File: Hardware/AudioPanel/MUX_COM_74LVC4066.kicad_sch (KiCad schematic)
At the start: 51 parts, among them SW10 ~{RESET}, SW11 ~{RESET}, SW12 ~{RESET}, SW13 ~{RESET}, SW14 ~{RESET}, SW15 ~{RESET}, SW9 ~{RESET}, U45 MCP23017_ML, U61 74LVC4066BQ, U62 74LVC4066BQ, U63 74LVC4066BQ, U64 74LVC4066BQ, U65 74LVC4066BQ, U66 74LVC4066BQ, U67 74LVC4066BQ, U68 74LVC4066BQ, U69 74LVC4066BQ, U70 74LVC4066BQ, U71 74LVC4066BQ, U72 74LVC4066BQ, U73 74LVC4066BQ, U74 74LVC4066BQ, U75 74LVC4066BQ, U76 74LVC4066BQ, U77 74LVC4066BQ, U78 74LVC4066BQ, U79 74LVC4066BQ, U80 74LVC4066BQ, U81 74LVC4066BQ, U82 74LVC4066BQ, U83 74LVC4066BQ, U84 74LVC4066BQ, U85 74LVC4066BQ, U86 74LVC4066BQ, U87 74LVC4066BQ, U88 74LVC4066BQ, U89 74LVC4066BQ, U90 74LVC4066BQ, U91 MCP23017_ML, U92 MCP23017_ML, U93 MCP23017_ML, U94 MCP23017_ML, U95 MCP23017_ML, U96 MCP23017_ML

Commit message: Added DSP chips, practicing with bus lines
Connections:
- net CTS_1 renamed CTS.1
- net CTS_2 renamed CTS.2
- net CTS_3 renamed CTS.3
- net CTS_4 renamed CTS.4
- net CTS_5 renamed CTS.5
- net RTS_1 renamed RTS.1
- net RTS_2 renamed RTS.2
- net RTS_3 renamed RTS.3
- net RTS_4 renamed RTS.4
- net RTS_5 renamed RTS.5
- net RXD_1 renamed RXD1
- net RXD_2 renamed RXD2
- net RXD_3 renamed RXD3
- net RXD_4 renamed RXD4
- net RXD_5 renamed RXD5
- net TXD_1 renamed TXD1
- net TXD_2 renamed TXD2
- net TXD_3 renamed TXD3
- net TXD_4 renamed TXD4
- net TXD_5 renamed TXD5

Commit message: Added group labels
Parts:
- removed U61, U62, U63, U64, U65, U66, U67, U68, U69, U70, U71, U72, U73, U74, U75, U76, U77, U78, U79, U80, U81, U82, U83, U84, U85, U86, U87, U88, U89, U90: 74LVC4066BQ, Package_SO:SO-14_3.9x8.65mm_P1.27mm, symbol Analog_Switch:CD4066BM
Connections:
- net CTS.1 renamed 480_COM.CTS
- net CTS.2 renamed 710_COM.CTS
- net CTS.3 renamed 700_COM.CTS
- net CTS.4 renamed EXTRA_COM.CTS
- net CTS.5 renamed PC_COM.CTS
- net RTS.1 renamed 480_COM.RTS
- net RTS.2 renamed 710_COM.RTS
- net RTS.3 renamed 700_COM.RTS
- net RTS.4 renamed EXTRA_COM.RTS
- net RTS.5 renamed PC_COM.RTS
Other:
- added sheet Switch Matrix (MATRIX_5X5.kicad_sch)
- moved on the sheet: C335, C336, C337, C338, C339, C340, C341, SW10, SW11, SW12, SW13, SW14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

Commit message: Simplified COM switching, added USB-232
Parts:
- removed C336, C337, C338, C339, C340: 100nF, symbol Device:C_Small
- removed SW10, SW11, SW12, SW13, SW14: ~{RESET}, Button_Switch_SMD:SW_SPST_TL3342, symbol Switch:SW_Push
- removed U91, U92, U93, U94, U95: MCP23017_ML, Package_DFN_QFN:QFN-28-1EP_6x6mm_P0.65mm_EP4.25x4.25mm, symbol Interface_Expansion:MCP23017_ML
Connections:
- net A10 is gone; now on net 480_COM.TX: U45.17 (GPA0)
- net A2 is gone; now on net 480_COM.RX: U45.25 (GPB0)
- net A3 is gone; now on net 710_COM.RX: U45.26 (GPB1)
- net A4 is gone; now on net 700_COM.RX: U45.27 (GPB2)
- net A5 is gone; now on net EXTRA_COM.RX: U45.28 (GPB3)
- net B1 is gone; now on net 710_COM.TX: U45.18 (GPA1)
- net B3 is gone; now on net 700_COM.TX: U45.19 (GPA2)
- net B4 is gone; now on net EXTRA_COM.TX: U45.20 (GPA3)
- net 480_COM.CTS: now also U96.17 (GPA0); no longer U96.25 (GPB0)
- net 480_COM.RTS: now also U96.25 (GPB0); no longer U96.17 (GPA0)
- net 700_COM.CTS: now also U96.19 (GPA2); no longer U96.27 (GPB2)
- net 700_COM.RTS: now also U96.27 (GPB2); no longer U96.19 (GPA2)
- net 710_COM.CTS: now also U96.18 (GPA1); no longer U96.26 (GPB1)
- net 710_COM.RTS: now also U96.26 (GPB1); no longer U96.18 (GPA1)
- net EXTRA_COM.CTS: now also U96.20 (GPA3); no longer U96.28 (GPB3)
- net EXTRA_COM.RTS: now also U96.28 (GPB3); no longer U96.20 (GPA3)
- net PC2_COM.RTS: now reaches U96.2 (GPB5)
- net PC2_COM.CTS: now reaches U96.22 (GPA5)
- net PC3_COM.CTS: now reaches U96.23 (GPA6)
- net PC4_COM.CTS: now reaches U96.24 (GPA7)
- net PC3_COM.RTS: now reaches U96.3 (GPB6)
- net PC4_COM.RTS: now reaches U96.4 (GPB7)
- net A6 renamed PC1_COM.RX
- net A7 renamed PC2_COM.RX
- net A8 renamed PC3_COM.RX
- net A9 renamed PC4_COM.RX
- net B5 renamed PC1_COM.TX
- net B6 renamed PC2_COM.TX
- net B7 renamed PC3_COM.TX
- net B8 renamed PC4_COM.TX
- net PC_COM.CTS renamed PC1_COM.RTS
- net PC_COM.RTS renamed PC1_COM.CTS
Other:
- removed sheet Switch Matrix
- moved on the sheet: C335, C341, SW15, SW9, U45, U96

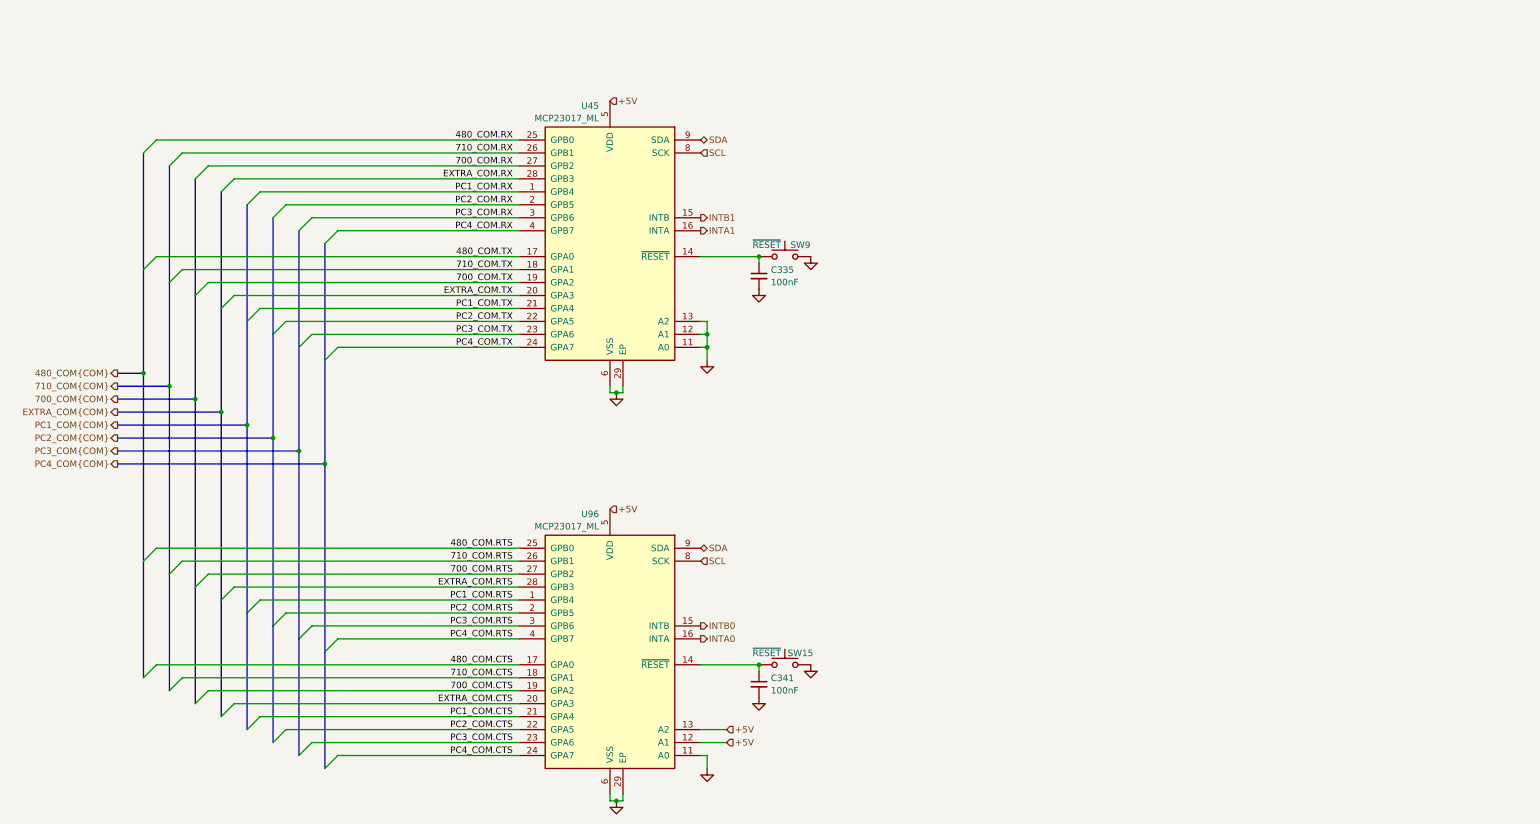
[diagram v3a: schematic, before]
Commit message: Added ideal diode controller to main power input
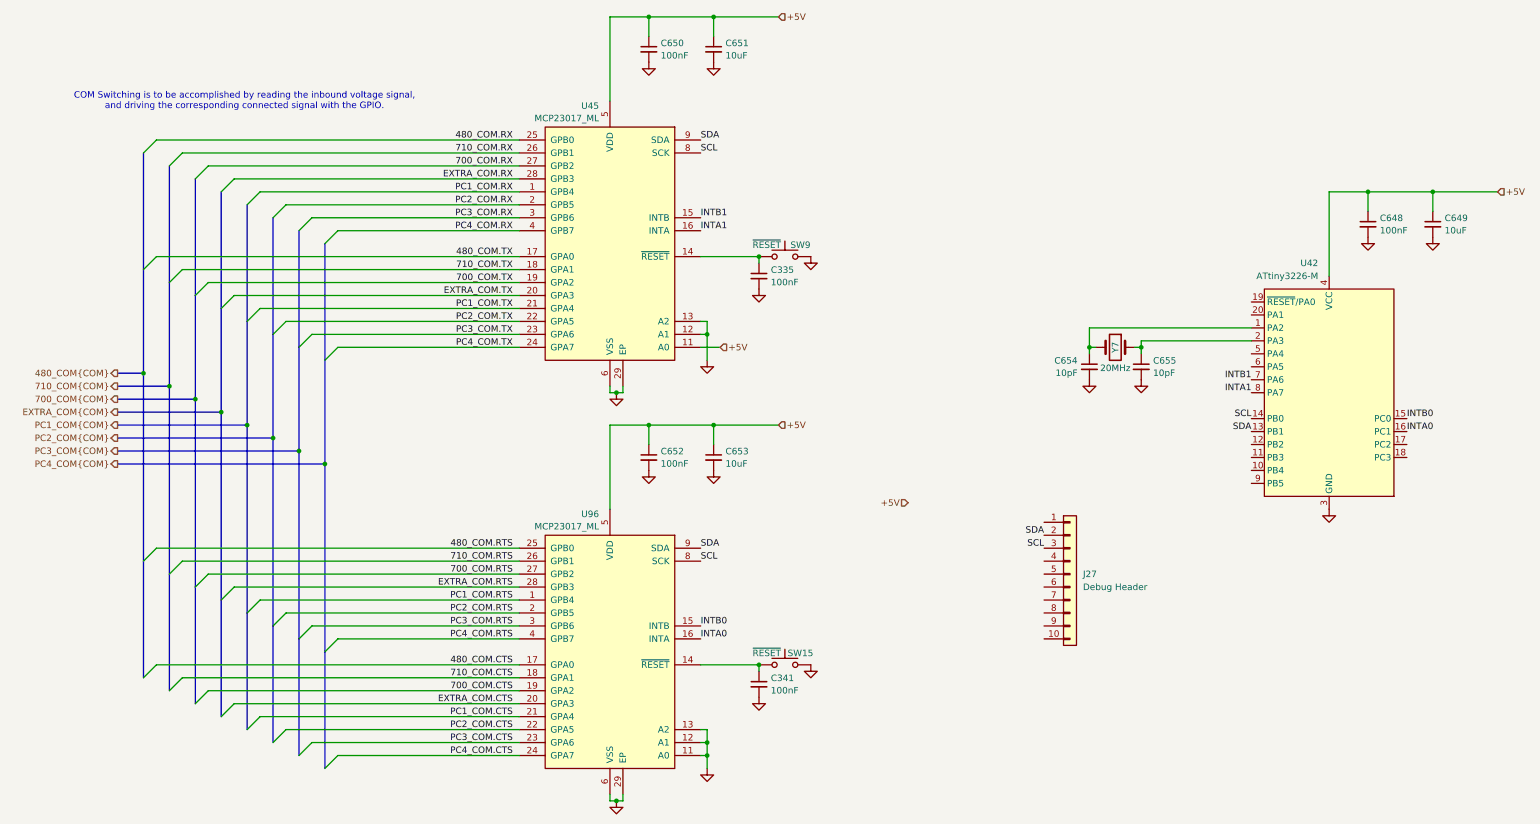
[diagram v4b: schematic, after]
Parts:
- added C648, C650, C652: 100nF, symbol Device:C_Small
- added C649, C651, C653: 10uF, symbol Device:C_Small
- added C654, C655: 10pF, symbol Device:C_Small
- added J27: Debug Header, symbol Connector_Generic:Conn_01x10
- added U42: ATtiny3226-M, Package_DFN_QFN:VQFN-20-1EP_3x3mm_P0.4mm_EP1.7x1.7mm, symbol MCU_Microchip_ATtiny:ATtiny3226-M
- added Y7: 20MHz, symbol Device:Crystal
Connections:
- net +5V: now also U45.11 (A0), C648.1, C649.1, C650.1, C651.1, C652.1, C653.1, U42.4 (VCC); no longer U96.12 (A1), U96.13 (A2)
- net GND: now also U96.12 (A1), U96.13 (A2), C648.2, C649.2, C650.2, C651.2, C652.2, C653.2, C654.2, C655.2, U42.21 (GND), U42.3 (GND); no longer U45.11 (A0)
- net INTA0: now also U42.16 (PC1)
- net INTA1: now also U42.8 (PA7)
- net INTB0: now also U42.15 (PC0)
- net INTB1: now also U42.7 (PA6)
- net SCL: now also J27.3 (Pin_3), U42.14 (PB0)
- net SDA: now also J27.2 (Pin_2), U42.13 (PB1)
- new net: C654.1, U42.1 (PA2), Y7.2
- new net: C655.1, U42.2 (PA3), Y7.1
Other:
- note added: "COM Switching is to be accomplished by reading the inbound voltage signal, and driving the corresponding connected signal with the GPIO."

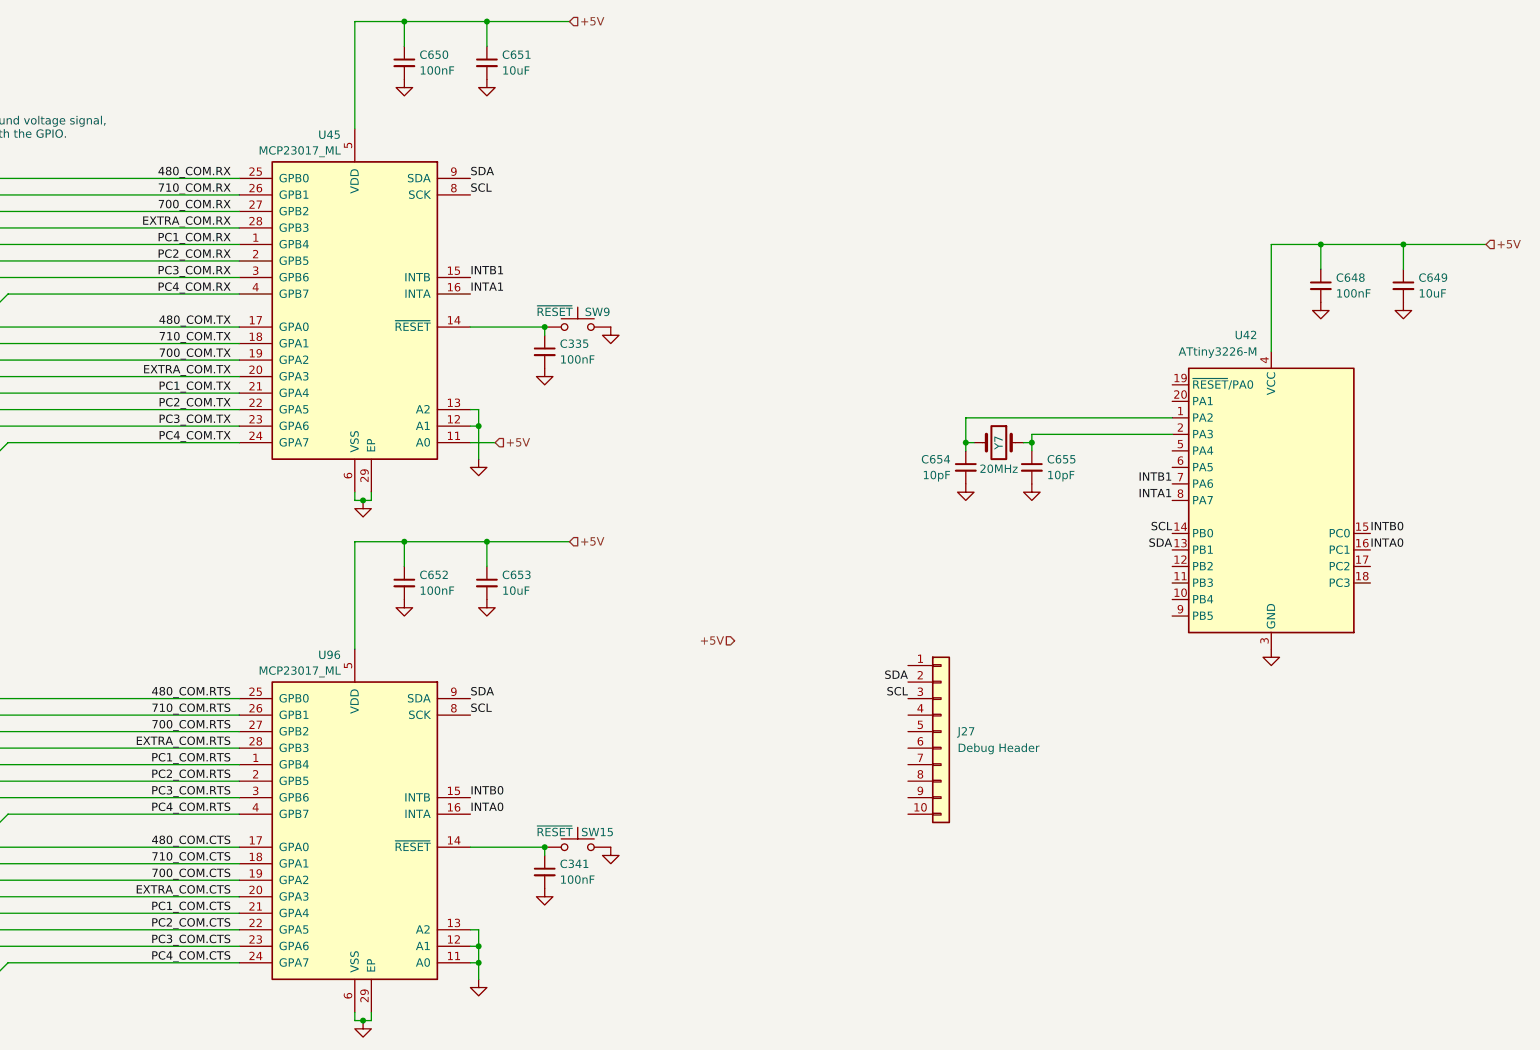
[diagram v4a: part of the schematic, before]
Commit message: Realized that I need to rethink how I'm going to mix the radio audio with the stereo audio
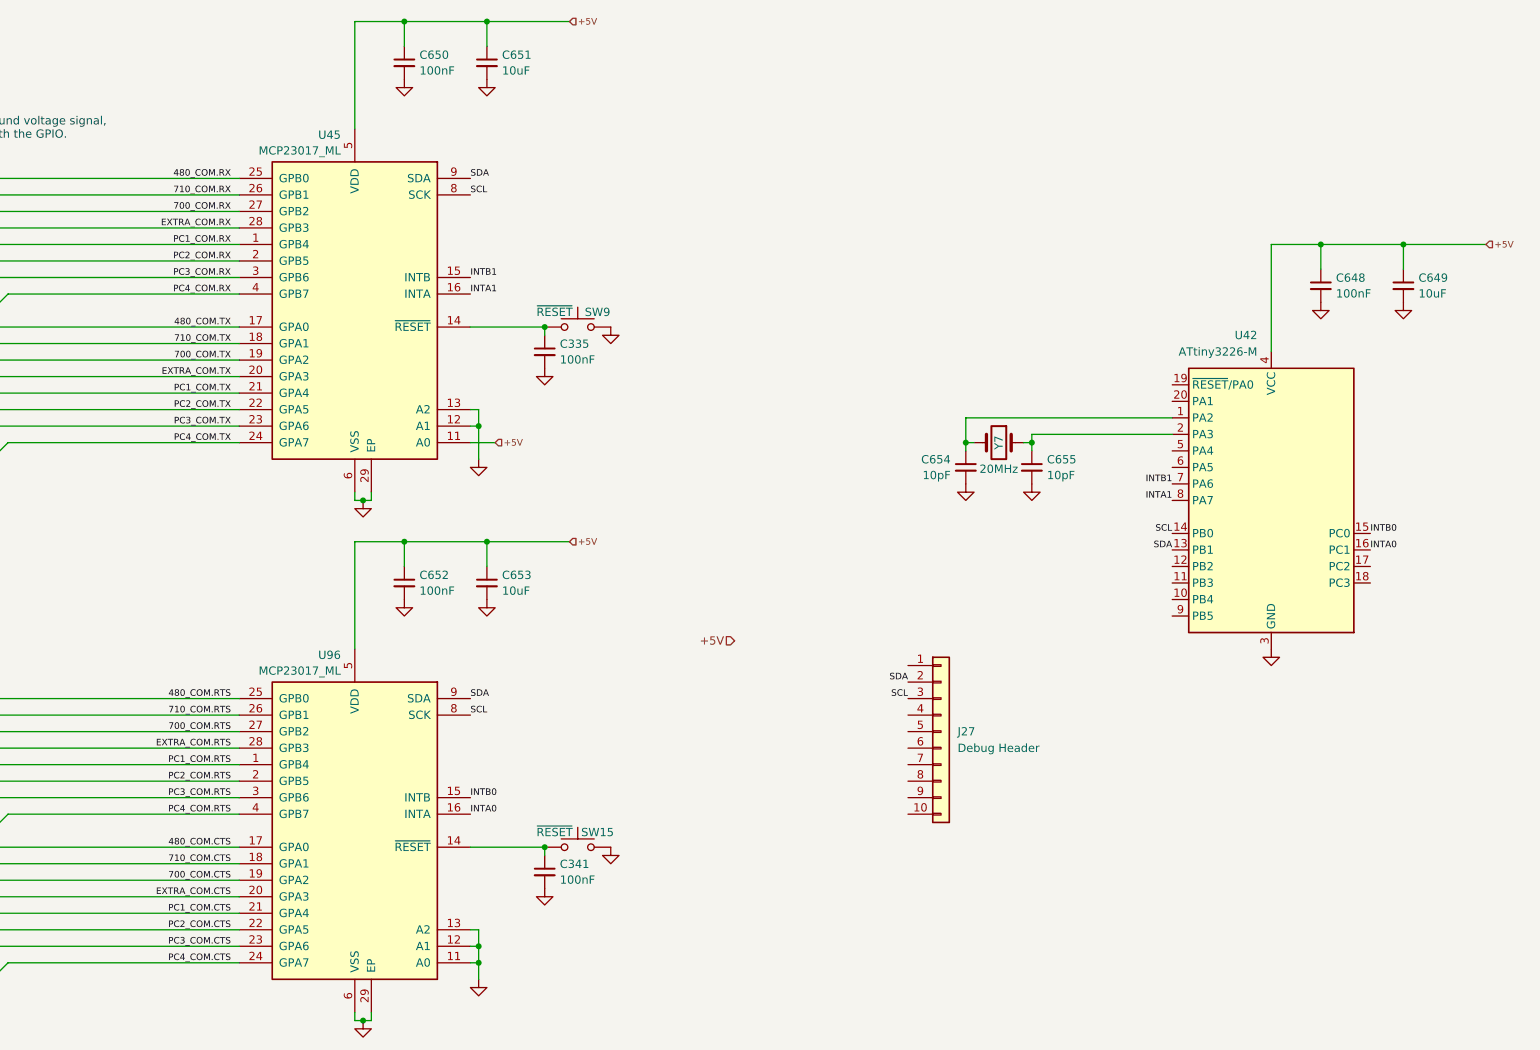
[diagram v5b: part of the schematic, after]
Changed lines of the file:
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@@
 		(effects
 			(font
-				(size 1.27 1.27)
+				(size 1 1)
 			)
 			(justify left bottom)
@@
 		(effects
 			(font
-				(size 1.27 1.27)
+				(size 1 1)
 			)
 			(justify right bottom)
@@
 		(effects
 			(font
-				(size 1.27 1.27)
+				(size 1 1)
 			)
 			(justify right bottom)
@@
 		(effects
 			(font
-				(size 1.27 1.27)
+				(size 1 1)
 			)
 			(justify right bottom)
@@
 		(effects
 			(font
-				(size 1.27 1.27)
+				(size 1 1)
 			)
 			(justify right bottom)
@@
 		(effects
 			(font
-				(size 1.27 1.27)
+				(size 1 1)
 			)
 			(justify right bottom)
@@
 		(effects
 			(font
-				(size 1.27 1.27)
+				(size 1 1)
 			)
 			(justify right bottom)
@@
 		(effects
 			(font
-				(size 1.27 1.27)
+				(size 1 1)
 			)
 			(justify right bottom)
@@
 		(effects
 			(font
-				(size 1.27 1.27)
+				(size 1 1)
 			)
 			(justify right bottom)
@@
 		(effects
 			(font
-				(size 1.27 1.27)
+				(size 1 1)
 			)
 			(justify right bottom)
@@
 		(effects
 			(font
-				(size 1.27 1.27)
+				(size 1 1)
 			)
 			(justify right bottom)
@@
 		(effects
 			(font
-				(size 1.27 1.27)
+				(size 1 1)
 			)
 			(justify right bottom)
@@
 		(effects
 			(font
-				(size 1.27 1.27)
+				(size 1 1)
 			)
 			(justify right bottom)
@@
 		(effects
 			(font
-				(size 1.27 1.27)
+				(size 1 1)
 			)
 			(justify right bottom)
@@
 		(effects
 			(font
-				(size 1.27 1.27)
+				(size 1 1)
 			)
 			(justify right bottom)
@@
 		(effects
 			(font
-				(size 1.27 1.27)
+				(size 1 1)
 			)
 			(justify right bottom)
@@
 		(effects
 			(font
-				(size 1.27 1.27)
+				(size 1 1)
 			)
 			(justify right bottom)
@@
 		(effects
 			(font
-				(size 1.27 1.27)
+				(size 1 1)
 			)
 			(justify left bottom)
@@
 		(effects
 			(font
-				(size 1.27 1.27)
+				(size 1 1)
 			)
 			(justify left bottom)
@@
 		(effects
 			(font
-				(size 1.27 1.27)
+				(size 1 1)
 			)
 			(justify right bottom)
@@
 		(effects
 			(font
-				(size 1.27 1.27)
+				(size 1 1)
 			)
 			(justify right bottom)
@@
 		(effects
 			(font
-				(size 1.27 1.27)
+				(size 1 1)
 			)
 			(justify right bottom)
@@
 		(effects
 			(font
-				(size 1.27 1.27)
+				(size 1 1)
 			)
 			(justify right bottom)
@@
 		(effects
 			(font
-				(size 1.27 1.27)
+				(size 1 1)
 			)
 			(justify right bottom)
@@
 		(effects
 			(font
-				(size 1.27 1.27)
+				(size 1 1)
 			)
 			(justify right bottom)
@@
 		(effects
 			(font
-				(size 1.27 1.27)
+				(size 1 1)
 			)
 			(justify right bottom)
@@
 		(effects
 			(font
-				(size 1.27 1.27)
+				(size 1 1)
 			)
 			(justify right bottom)
@@
 		(effects
 			(font
-				(size 1.27 1.27)
+				(size 1 1)
 			)
 			(justify right bottom)
@@
 		(effects
 			(font
-				(size 1.27 1.27)
+				(size 1 1)
 			)
 			(justify left bottom)
@@
 		(effects
 			(font
-				(size 1.27 1.27)
+				(size 1 1)
 			)
 			(justify right bottom)
@@
 		(effects
 			(font
-				(size 1.27 1.27)
+				(size 1 1)
 			)
 			(justify right bottom)
@@
 		(effects
 			(font
-				(size 1.27 1.27)
+				(size 1 1)
 			)
 			(justify left bottom)
@@
 		(effects
 			(font
-				(size 1.27 1.27)
+				(size 1 1)
 			)
 			(justify left bottom)
@@
 		(effects
 			(font
-				(size 1.27 1.27)
+				(size 1 1)
 			)
 			(justify right bottom)
@@
 		(effects
 			(font
-				(size 1.27 1.27)
+				(size 1 1)
 			)
 			(justify left bottom)
@@
 		(effects
 			(font
-				(size 1.27 1.27)
+				(size 1 1)
 			)
 			(justify right bottom)
@@
 		(effects
 			(font
-				(size 1.27 1.27)
+				(size 1 1)
 			)
 			(justify right bottom)
@@
 		(effects
 			(font
-				(size 1.27 1.27)
+				(size 1 1)
 			)
 			(justify right bottom)
@@
 		(effects
 			(font
-				(size 1.27 1.27)
+				(size 1 1)
 			)
 			(justify left bottom)
@@
 		(effects
 			(font
-				(size 1.27 1.27)
+				(size 1 1)
 			)
 			(justify right bottom)
@@
 		(effects
 			(font
-				(size 1.27 1.27)
+				(size 1 1)
 			)
 			(justify right bottom)
@@
 		(effects
 			(font
-				(size 1.27 1.27)
+				(size 1 1)
 			)
 			(justify right bottom)
@@
 		(effects
 			(font
-				(size 1.27 1.27)
+				(size 1 1)
 			)
 			(justify right bottom)
@@
 		(effects
 			(font
-				(size 1.27 1.27)
+				(size 1 1)
 			)
 			(justify right bottom)
@@
 		(effects
 			(font
-				(size 1.27 1.27)
+				(size 1 1)
 			)
 			(justify right bottom)
@@
 		(effects
 			(font
-				(size 1.27 1.27)
+				(size 1 1)
 			)
 			(justify left bottom)
@@
 		(effects
 			(font
-				(size 1.27 1.27)
+				(size 1 1)
 			)
 			(justify right bottom)
@@
 		(effects
 			(font
-				(size 1.27 1.27)
+				(size 1 1)
 			)
 			(justify left bottom)
@@
 		(effects
 			(font
-				(size 1.27 1.27)
+				(size 1 1)
 			)
 			(justify left)
@@
 		(effects
 			(font
-				(size 1.27 1.27)
+				(size 1 1)
 			)
 			(justify left)
@@
 		(effects
 			(font
-				(size 1.27 1.27)
+				(size 1 1)
 			)
 			(justify left)
@@
 		(effects
 			(font
-				(size 1.27 1.27)
+				(size 1 1)
 			)
 			(justify left)
